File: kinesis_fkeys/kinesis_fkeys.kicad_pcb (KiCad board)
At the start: 0 parts

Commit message: created basic shape for the pcb
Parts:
- added J1: RIGHT_13_TOP, dodo_conn:Molex-39-53-2135, F.Cu at (64.3, 89.4)
- added J2: LEFT_13_TOP, dodo_conn:Molex-39-53-2135, F.Cu at (112.6, 89.4)
- added S1: ML1A-11JW, dodo_button_and_switch:ML1A11JW, F.Cu at (63.1, 45.9)
- added S10: ML1A-11JW, dodo_button_and_switch:ML1A11JW, F.Cu at (111.4, 45.9)
- added S11: ML1A-11JW, dodo_button_and_switch:ML1A11JW, F.Cu at (111.4, 60.4)
- added S12: ML1A-11JW, dodo_button_and_switch:ML1A11JW, F.Cu at (111.4, 74.9)
- added S13: ML1A-11JW, dodo_button_and_switch:ML1A11JW, F.Cu at (126.8, 45.9)
- added S14: ML1A-11JW, dodo_button_and_switch:ML1A11JW, F.Cu at (126.8, 60.4)
- added S15: ML1A-11JW, dodo_button_and_switch:ML1A11JW, F.Cu at (126.8, 74.9)
- added S16: ML1A-11JW, dodo_button_and_switch:ML1A11JW, F.Cu at (142.2, 45.9)
- added S17: ML1A-11JW, dodo_button_and_switch:ML1A11JW, F.Cu at (142.2, 60.4)
- added S18: ML1A-11JW, dodo_button_and_switch:ML1A11JW, F.Cu at (142.2, 74.9)
- added S2: ML1A-11JW, dodo_button_and_switch:ML1A11JW, F.Cu at (63.1, 60.4)
- added S3: ML1A-11JW, dodo_button_and_switch:ML1A11JW, F.Cu at (63.1, 74.9)
- added S4: ML1A-11JW, dodo_button_and_switch:ML1A11JW, F.Cu at (78.5, 45.9)
- added S5: ML1A-11JW, dodo_button_and_switch:ML1A11JW, F.Cu at (78.5, 60.4)
- added S6: ML1A-11JW, dodo_button_and_switch:ML1A11JW, F.Cu at (78.5, 74.9)
- added S7: ML1A-11JW, dodo_button_and_switch:ML1A11JW, F.Cu at (93.9, 45.9)
- added S8: ML1A-11JW, dodo_button_and_switch:ML1A11JW, F.Cu at (93.9, 60.4)
- added S9: ML1A-11JW, dodo_button_and_switch:ML1A11JW, F.Cu at (93.9, 74.9)
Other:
- board outline added: 123.3 x 26.6 mm
- copper layers 0 -> 2

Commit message: modified pcb cut edge
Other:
- board size 123.3 x 26.6 mm -> 123 x 26 mm
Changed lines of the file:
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@@
   (setup
     (pad_to_mask_clearance 0)
-    (grid_origin 48.195 125.84)
+    (grid_origin 48.195 128.34)
     (pcbplotparams
       (layerselection 0x00010fc_ffffffff)
@@
     )
   )
-  (gr_arc (start 60.87 151.125) (mid 61.771561 151.498439) (end 62.145 152.4)
-    (stroke (width 1) (type default)) (layer "Edge.Cuts"))
-  (gr_arc (start 155.71 131.325) (mid 156.91 132.525) (end 155.71 133.725)
+  (gr_line (start 171.195 128.34) (end 171.195 153.34)
     (stroke (width 0.1) (type default)) (layer "Edge.Cuts"))
-  (gr_line (start 60.87 151.125) (end 48.21 151.125)
-    (stroke (width 1) (type default)) (layer "Edge.Cuts"))
-  (gr_arc (start 69.16 133.725) (mid 67.96 132.525) (end 69.16 131.325)
+  (gr_line (start 158.195 154.34) (end 48.195 154.34)
     (stroke (width 0.1) (type default)) (layer "Edge.Cuts"))
-  (gr_line (start 48.195 125.84) (end 171.535 125.84)
-    (stroke (width 1) (type default)) (layer "Edge.Cuts"))
-  (gr_line (start 62.145 152.4) (end 171.535 152.4)
-    (stroke (width 1) (type default)) (layer "Edge.Cuts"))
-  (gr_arc (start 75.035 131.325) (mid 76.235 132.525) (end 75.035 133.725)
+  (gr_line (start 139.945 132.34) (end 145.945 132.34)
     (stroke (width 0.1) (type default)) (layer "Edge.Cuts"))
-  (gr_line (start 149.835 131.325) (end 155.71 131.325)
+  (gr_arc (start 158.195 154.34) (mid 158.487893 153.632893) (end 159.195 153.34)
     (stroke (width 0.1) (type default)) (layer "Edge.Cuts"))
-  (gr_line (start 92.785 131.325) (end 98.16 131.325)
+  (gr_line (start 55.445 129.84) (end 61.445 129.84)
     (stroke (width 0.1) (type default)) (layer "Edge.Cuts"))
-  (gr_line (start 149.835 133.725) (end 155.685 133.725)
+  (gr_line (start 48.195 128.34) (end 171.195 128.34)
     (stroke (width 0.1) (type default)) (layer "Edge.Cuts"))
-  (gr_line (start 92.785 133.725) (end 98.16 133.725)
+  (gr_line (start 159.195 153.34) (end 171.195 153.34)
     (stroke (width 0.1) (type default)) (layer "Edge.Cuts"))
-  (gr_arc (start 149.835 133.725) (mid 148.635 132.525) (end 149.835 131.325)
+  (gr_line (start 105.945 132.34) (end 111.945 132.34)
     (stroke (width 0.1) (type default)) (layer "Edge.Cuts"))
-  (gr_line (start 69.16 131.325) (end 75.035 131.325)
+  (gr_arc (start 105.945 132.34) (mid 104.695 131.09) (end 105.945 129.84)
     (stroke (width 0.1) (type default)) (layer "Edge.Cuts"))
-  (gr_line (start 69.16 133.725) (end 75.01 133.725)
+  (gr_line (start 48.195 154.34) (end 48.195 128.34)
     (stroke (width 0.1) (type default)) (layer "Edge.Cuts"))
-  (gr_arc (start 98.16 131.325) (mid 99.36 132.525) (end 98.16 133.725)
+  (gr_arc (start 55.445 132.34) (mid 54.195 131.09) (end 55.445 129.84)
     (stroke (width 0.1) (type default)) (layer "Edge.Cuts"))
-  (gr_line (start 48.195 125.84) (end 48.21 151.125)
-    (stroke (width 1) (type default)) (layer "Edge.Cuts"))
-  (gr_arc (start 92.785 133.725) (mid 91.585 132.525) (end 92.785 131.325)
+  (gr_arc (start 111.945 129.84) (mid 113.195 131.09) (end 111.945 132.34)
     (stroke (width 0.1) (type default)) (layer "Edge.Cuts"))
-  (gr_line (start 171.535 152.4) (end 171.535 125.84)
-    (stroke (width 1) (type default)) (layer "Edge.Cuts"))
+  (gr_line (start 139.945 129.84) (end 145.945 129.84)
+    (stroke (width 0.1) (type default)) (layer "Edge.Cuts"))
+  (gr_line (start 105.945 129.84) (end 111.945 129.84)
+    (stroke (width 0.1) (type default)) (layer "Edge.Cuts"))
+  (gr_arc (start 145.945 129.84) (mid 147.195 131.09) (end 145.945 132.34)
+    (stroke (width 0.1) (type default)) (layer "Edge.Cuts"))
+  (gr_arc (start 139.945 132.34) (mid 138.695 131.09) (end 139.945 129.84)
+    (stroke (width 0.1) (type default)) (layer "Edge.Cuts"))
+  (gr_line (start 55.445 132.34) (end 61.445 132.34)
+    (stroke (width 0.1) (type default)) (layer "Edge.Cuts"))
+  (gr_arc (start 61.445 129.84) (mid 62.695 131.09) (end 61.445 132.34)
+    (stroke (width 0.1) (type default)) (layer "Edge.Cuts"))
 )

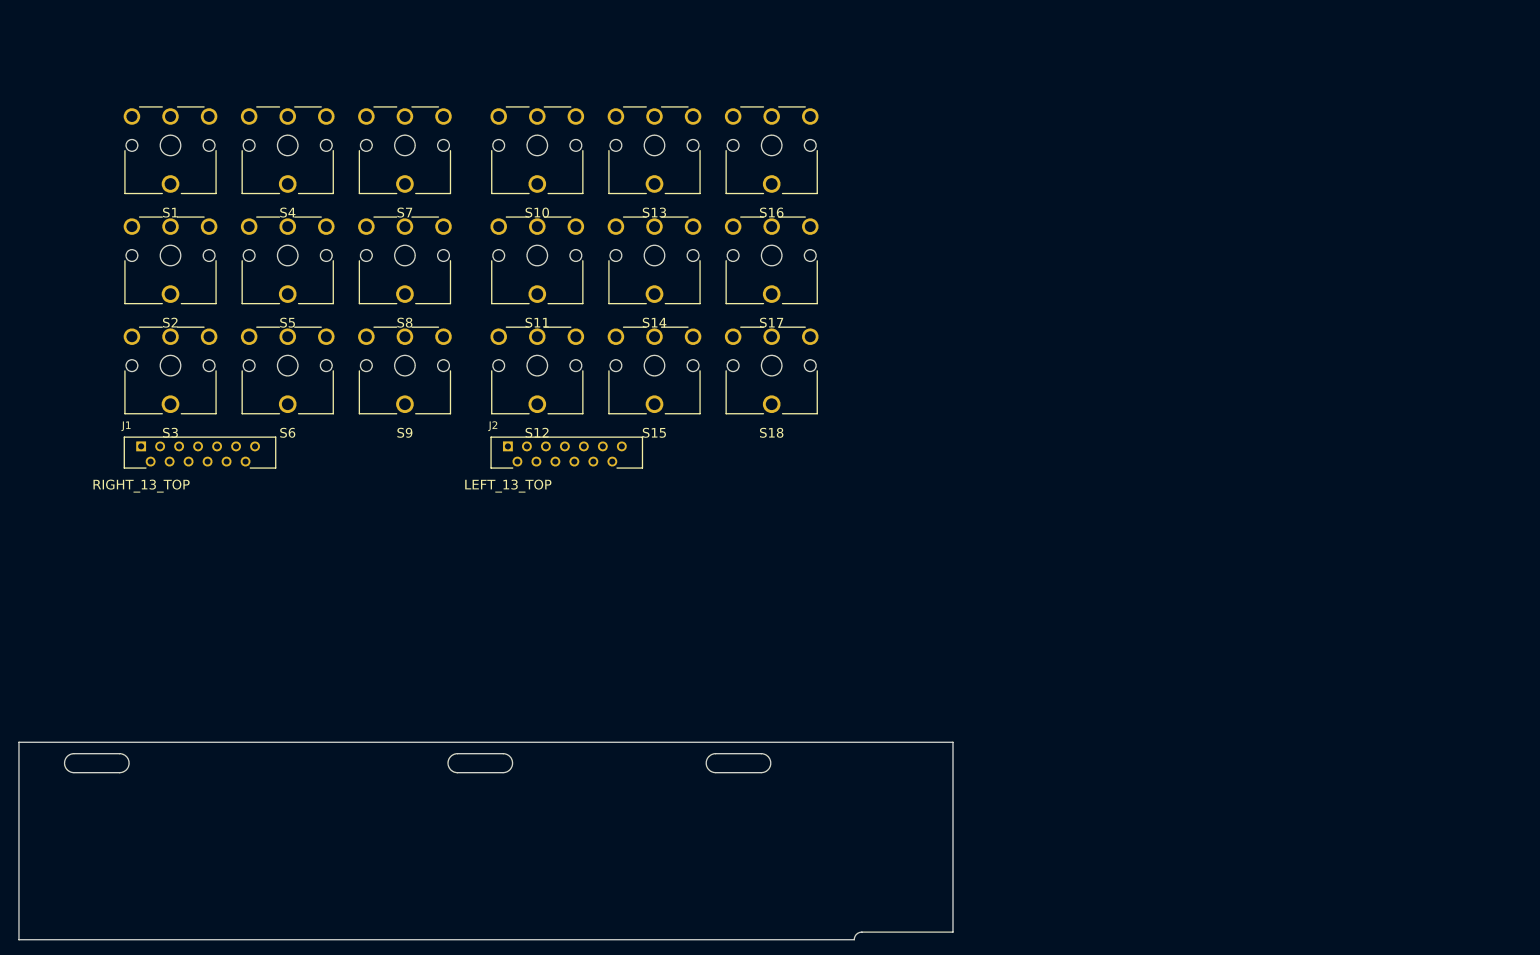
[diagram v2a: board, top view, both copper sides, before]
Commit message: buttons schematics verified and placed on the pcb on exact spots
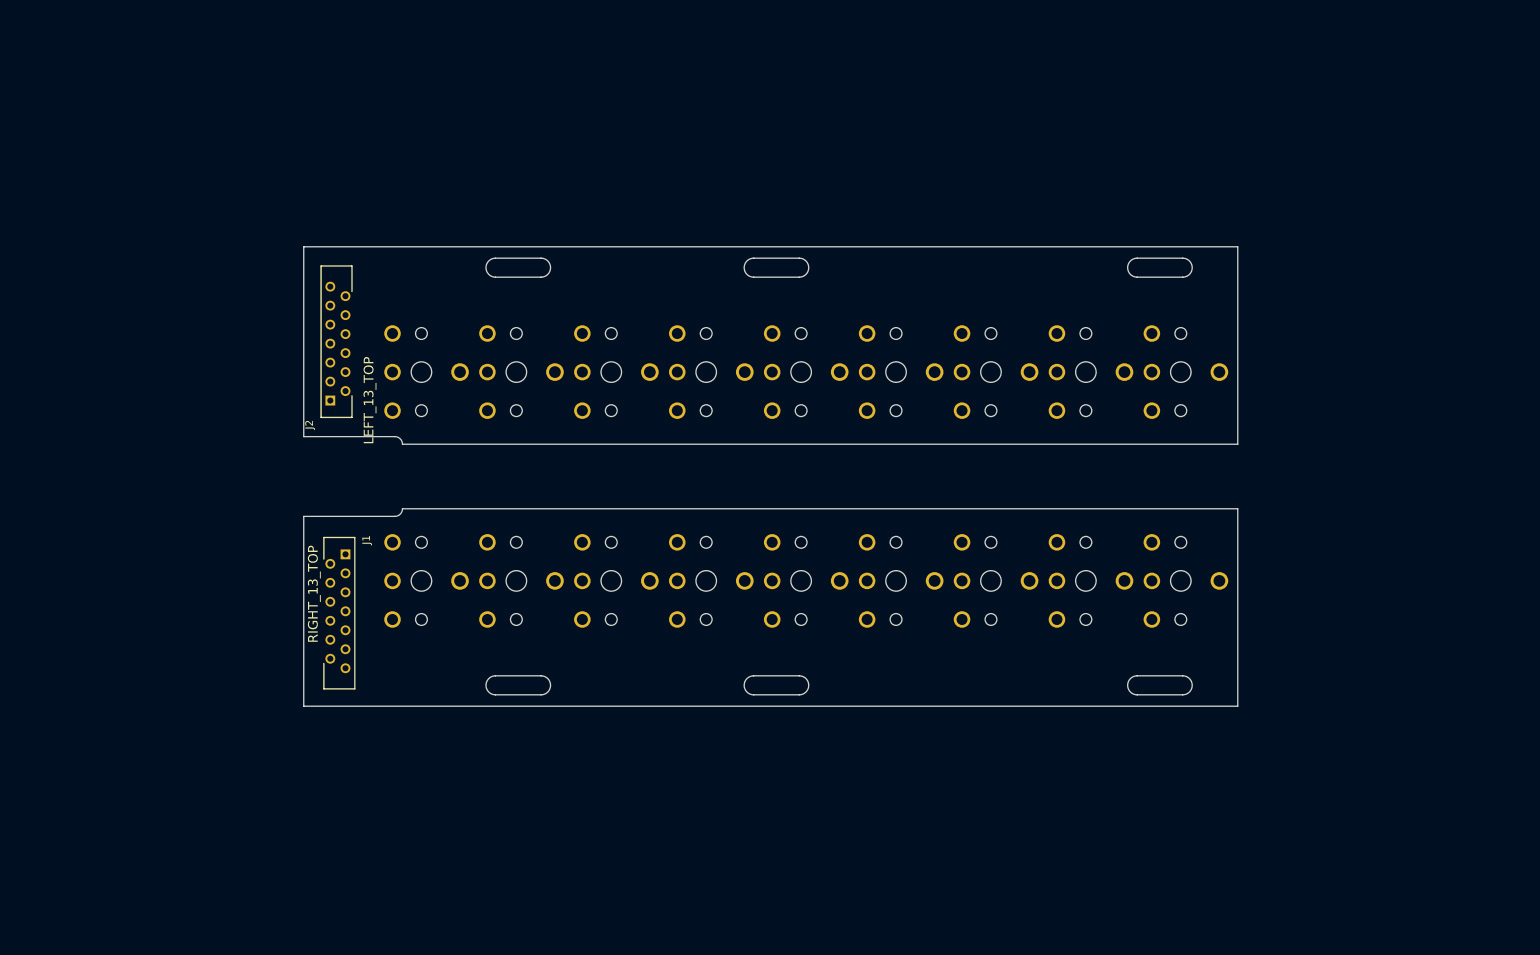
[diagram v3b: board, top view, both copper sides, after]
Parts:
- S1, S10, S11, S12, S13, S14, S15, S16, S17, S18, S2, S3, S4, S5, S6, S7, S8, S9: moved to B.Cu
- moved S1 145.6 mm to (197.4, 102.0), turned to -90 degrees
- moved S2 128.7 mm to (184.9, 102.0), turned to -90 degrees
- moved S3 112.6 mm to (172.4, 102.0), turned to -90 degrees
- moved S4 98.8 mm to (159.9, 102.0), turned to -90 degrees
- moved S10 90.6 mm to (197.4, 74.5), turned to -90 degrees
- moved S5 80.5 mm to (147.4, 102.0), turned to -90 degrees
- moved S7 62.9 mm to (122.4, 102.0), turned to -90 degrees
- moved S6 62.5 mm to (134.9, 102.0), turned to -90 degrees
- moved S8 44.5 mm to (109.9, 102.0), turned to -90 degrees
- moved S18 42.6 mm to (184.9, 74.5), turned to -90 degrees
- moved S16 33.6 mm to (159.9, 74.5), turned to -90 degrees
- moved S17 33.3 mm to (172.4, 74.5), turned to -90 degrees
- moved J1 30.4 mm to (91.2, 103.6), turned to -90 degrees
- moved S13 28.9 mm to (122.4, 74.5), turned to -90 degrees
- moved S9 27.3 mm to (97.4, 102.0), turned to -90 degrees
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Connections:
- J1 pad 13: GND -> /right_fkeys/ROW_F1
- J1 pad 3: GND -> /right_fkeys/ROW_F1
- J1 pad 6: GND -> /right_fkeys/ROW_F1
- S1 pad 2: GND -> /right_fkeys/ROW_F1
- S5 pad 2: GND -> /right_fkeys/ROW_F1
- S8 pad 2: GND -> /right_fkeys/ROW_F1
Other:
- board size 123 x 26 mm -> 123 x 60.5 mm

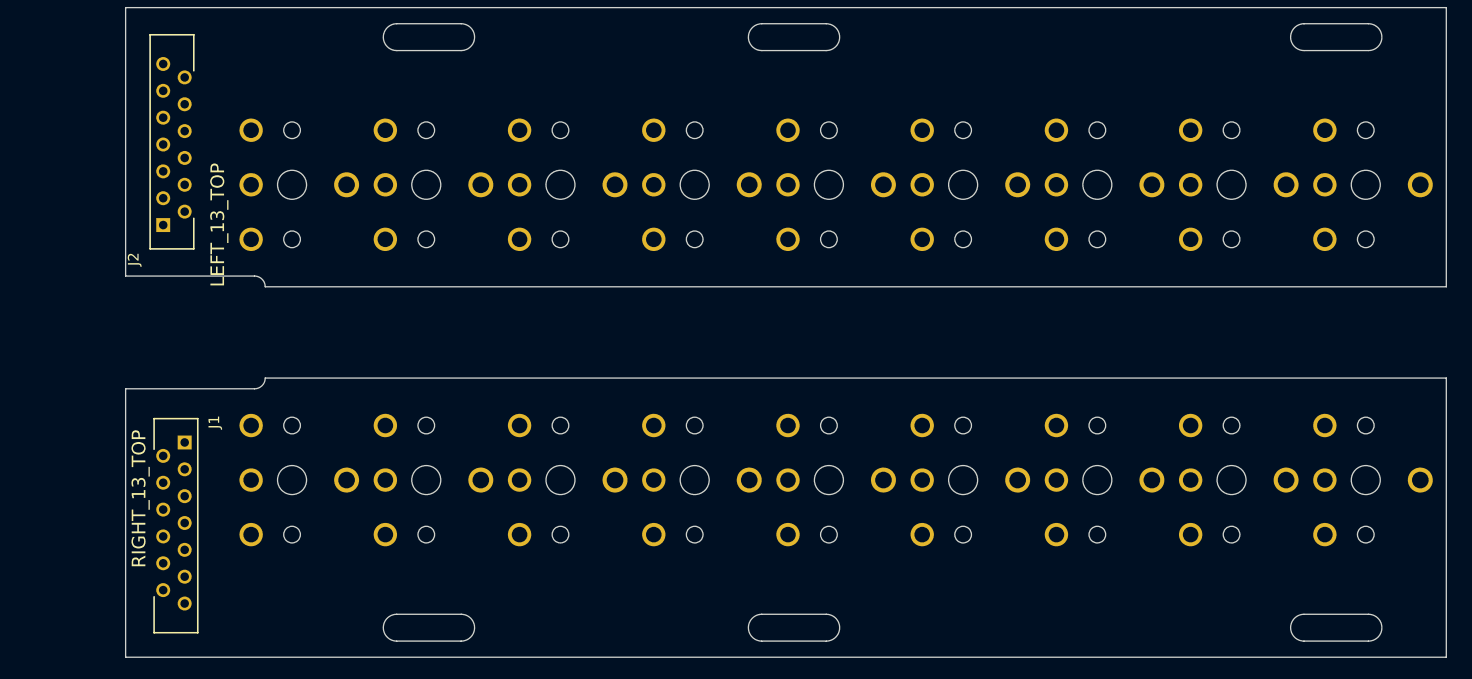
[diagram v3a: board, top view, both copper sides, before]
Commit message: added TE 84953 6 pin connectors to reduce amount of tracks
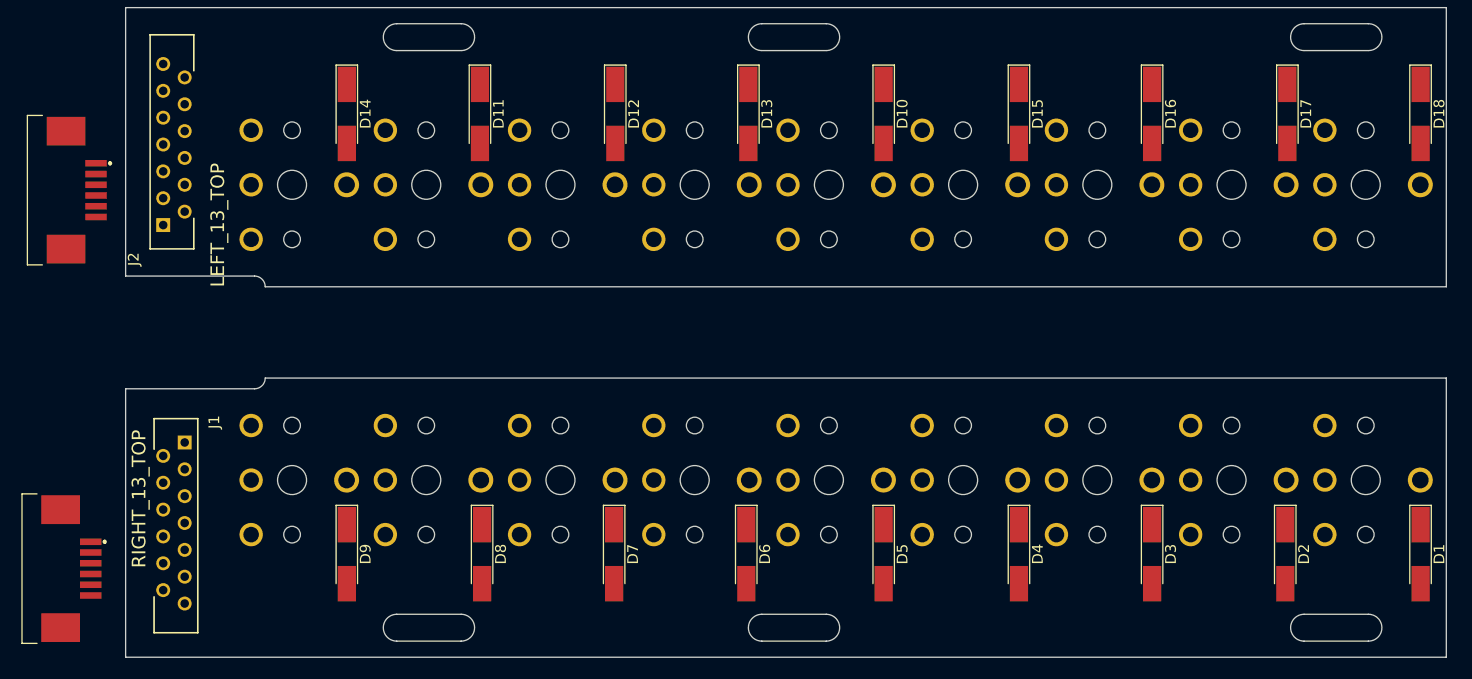
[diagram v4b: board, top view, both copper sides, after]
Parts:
- added D1: D, Diode_SMD:D_MiniMELF_Handsoldering, F.Cu at (206.3, 114.0)
- added D10: D, Diode_SMD:D_MiniMELF_Handsoldering, F.Cu at (156.3, 73.0)
- added D11: D, Diode_SMD:D_MiniMELF_Handsoldering, F.Cu at (118.7, 73.0)
- added D12: D, Diode_SMD:D_MiniMELF_Handsoldering, F.Cu at (131.3, 73.0)
- added D13: D, Diode_SMD:D_MiniMELF_Handsoldering, F.Cu at (143.7, 73.0)
- added D14: D, Diode_SMD:D_MiniMELF_Handsoldering, F.Cu at (106.3, 73.0)
- added D15: D, Diode_SMD:D_MiniMELF_Handsoldering, F.Cu at (168.9, 73.0)
- added D16: D, Diode_SMD:D_MiniMELF_Handsoldering, F.Cu at (181.3, 73.0)
- added D17: D, Diode_SMD:D_MiniMELF_Handsoldering, F.Cu at (193.9, 73.0)
- added D18: D, Diode_SMD:D_MiniMELF_Handsoldering, F.Cu at (206.3, 73.0)
- added D2: D, Diode_SMD:D_MiniMELF_Handsoldering, F.Cu at (193.7, 114.0)
- added D3: D, Diode_SMD:D_MiniMELF_Handsoldering, F.Cu at (181.3, 114.0)
- added D4: D, Diode_SMD:D_MiniMELF_Handsoldering, F.Cu at (168.9, 114.0)
- added D5: D, Diode_SMD:D_MiniMELF_Handsoldering, F.Cu at (156.3, 114.0)
- added D6: D, Diode_SMD:D_MiniMELF_Handsoldering, F.Cu at (143.5, 114.0)
- added D7: D, Diode_SMD:D_MiniMELF_Handsoldering, F.Cu at (131.2, 114.0)
- added D8: D, Diode_SMD:D_MiniMELF_Handsoldering, F.Cu at (118.9, 114.0)
- added D9: D, Diode_SMD:D_MiniMELF_Handsoldering, F.Cu at (106.3, 114.0)
- added J3: Conn_01x06, dodo_conn:84953-6, F.Cu at (79.9, 115.3)
- added J4: Conn_01x06, dodo_conn:84953-6, F.Cu at (80.4, 80.1)
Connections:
- S1 pad 4: /right_fkeys/COL_5 -> Net-(D1-K)
- S10 pad 4: /left_fkeys/COL_0 -> Net-(D18-A)
- S11 pad 4: /left_fkeys/COL_2 -> Net-(D14-A)
- S12 pad 4: /left_fkeys/COL_2 -> Net-(D11-A)
- S13 pad 4: /left_fkeys/COL_2 -> Net-(D12-A)
- S14 pad 4: /left_fkeys/COL_1 -> Net-(D13-A)
- S15 pad 4: /left_fkeys/COL_1 -> Net-(D10-A)
- S16 pad 4: /left_fkeys/COL_1 -> Net-(D15-A)
- S17 pad 4: /left_fkeys/COL_0 -> Net-(D16-A)
- S18 pad 4: /left_fkeys/COL_0 -> Net-(D17-A)
- S2 pad 4: /right_fkeys/COL_5 -> Net-(D2-K)
- S3 pad 4: /right_fkeys/COL_5 -> Net-(D3-K)
- S4 pad 4: /right_fkeys/COL_4 -> Net-(D4-K)
- S5 pad 4: /right_fkeys/COL_4 -> Net-(D5-K)
- S6 pad 4: /right_fkeys/COL_4 -> Net-(D6-K)
- S7 pad 4: /right_fkeys/COL_3 -> Net-(D7-K)
- S8 pad 4: /right_fkeys/COL_3 -> Net-(D8-K)
- S9 pad 4: /right_fkeys/COL_3 -> Net-(D9-K)
